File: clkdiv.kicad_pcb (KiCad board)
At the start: 2 copper layers, 11 parts, among them J1 Conn_02x05_Odd_Even

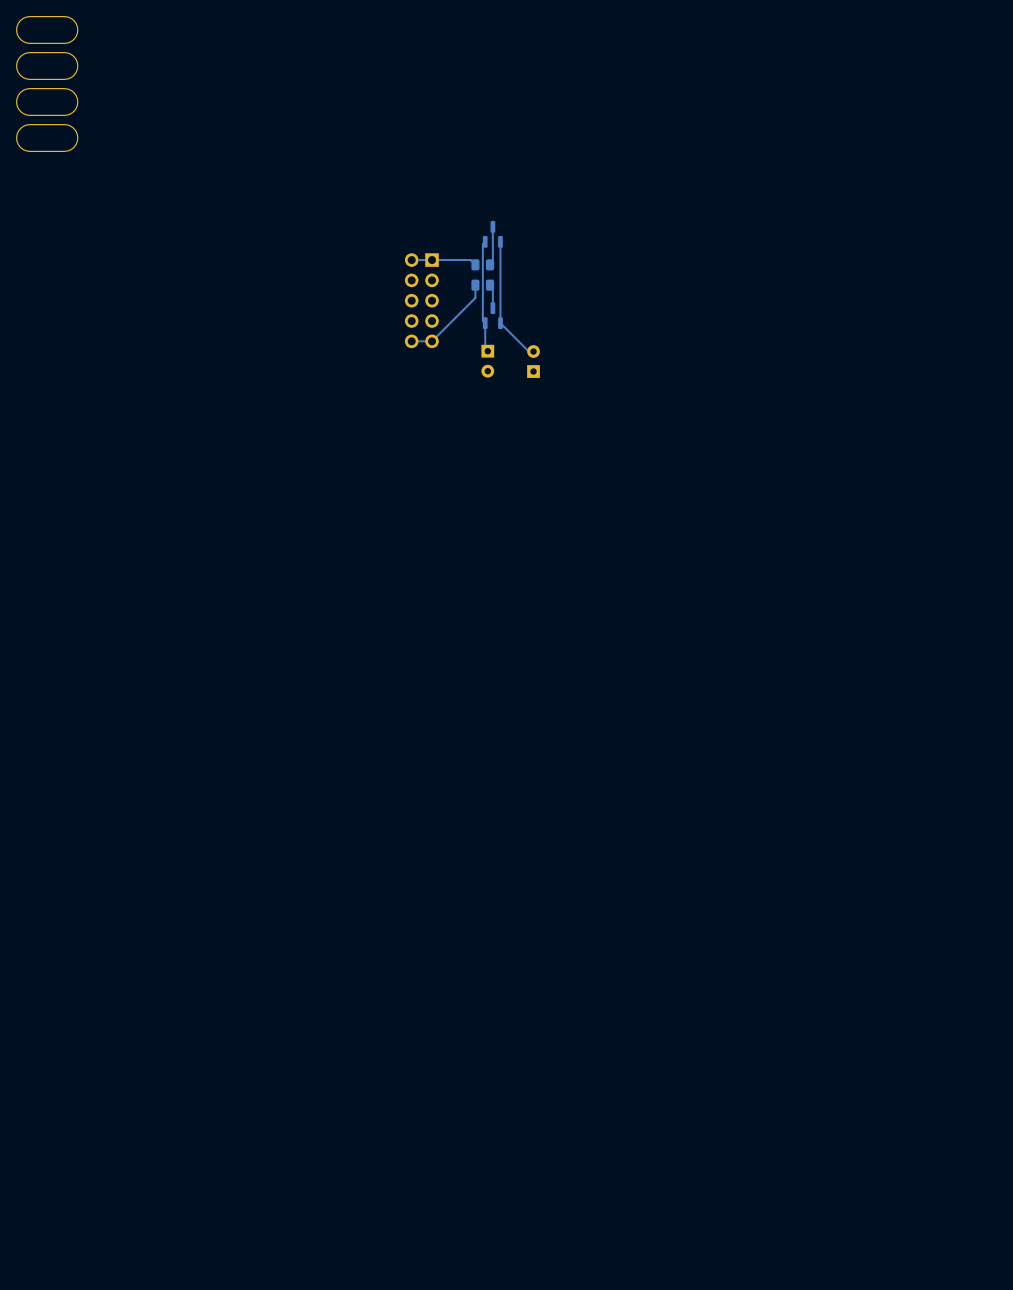
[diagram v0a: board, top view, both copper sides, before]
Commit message: pcb laid out, bom generated
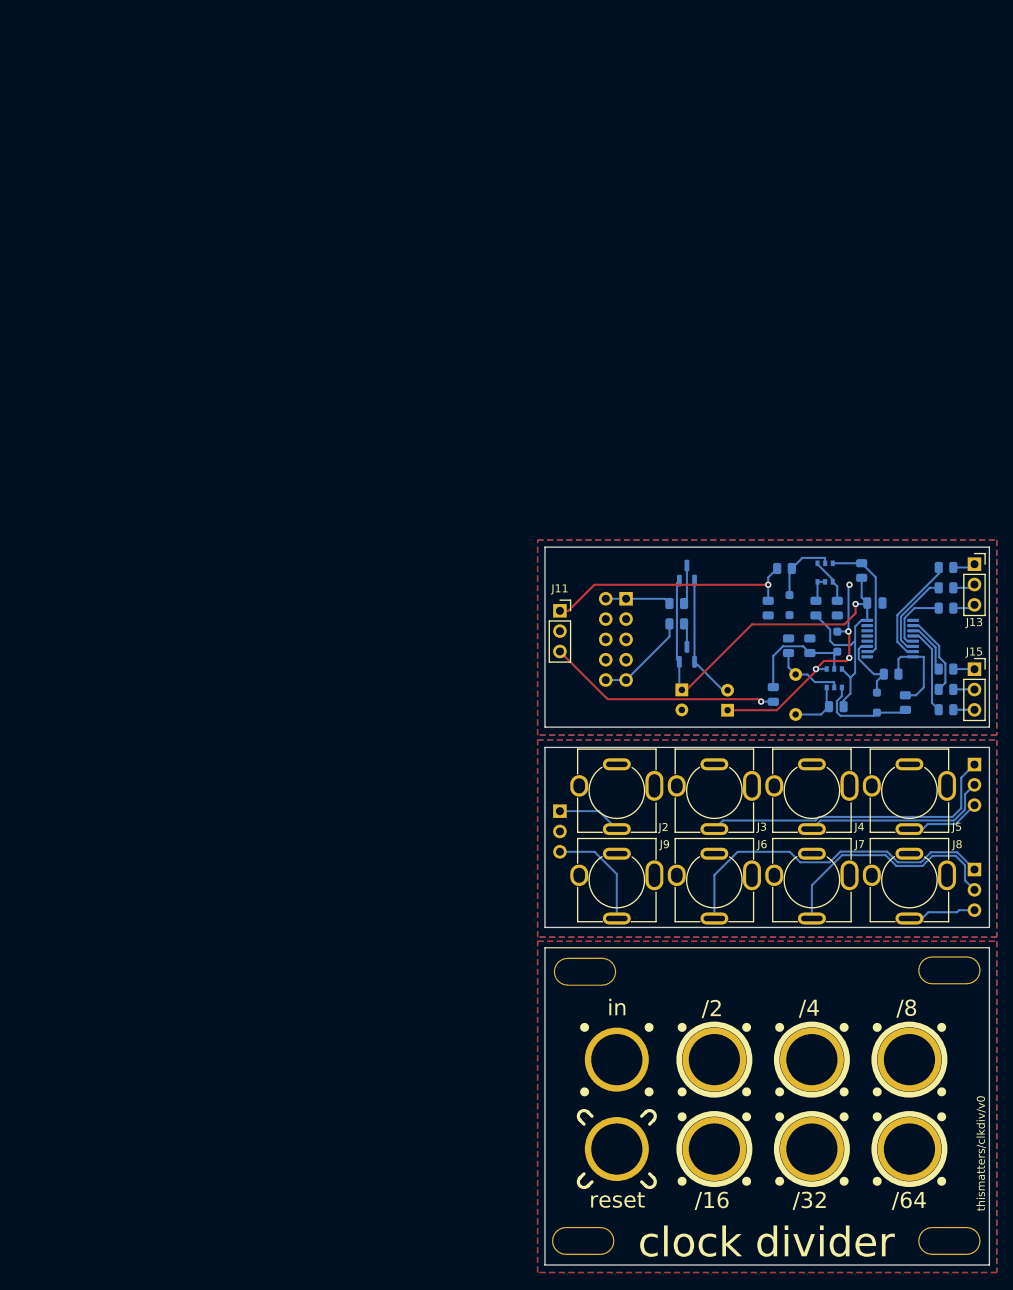
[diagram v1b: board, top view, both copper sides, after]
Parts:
- added C3: 100n, Capacitor_SMD:C_0805_2012Metric, B.Cu at (140.5, 88.6)
- added C4: 47n box, Capacitor_THT:C_Rect_L7.2mm_W2.5mm_P5.00mm_FKS2_FKP2_MKS2_MKP2, B.Cu at (130.6, 102.6)
- added D3: 1N4148, Diode_SMD:D_SOD-323_HandSoldering, B.Cu at (129.8, 88.9)
- added D4: 1N4148, Diode_SMD:D_SOD-323_HandSoldering, B.Cu at (135.8, 93.5)
- added D5: 1N4148, Diode_SMD:D_SOD-323_HandSoldering, B.Cu at (140.7, 101.1)
- added H10: 1/32, Eurorack:Mech-AudioJack-Hole-Output-Clock, F.Cu at (132.6, 156.9)
- added H11: 1/64, Eurorack:Mech-AudioJack-Hole-Output-Clock, F.Cu at (144.8, 156.9)
- added H12: reset, Eurorack:Mech-AudioJack-Hole-Input-Gate, F.Cu at (108.2, 156.9)
- added H5: in, Eurorack:Mech-AudioJack-Hole-Input-Clock, F.Cu at (108.2, 145.7)
- added H6: 1/2, Eurorack:Mech-AudioJack-Hole-Output-Clock, F.Cu at (120.4, 145.7)
- added H7: 1/4, Eurorack:Mech-AudioJack-Hole-Output-Clock, F.Cu at (132.6, 145.7)
- added H8: 1/8, Eurorack:Mech-AudioJack-Hole-Output-Clock, F.Cu at (144.8, 145.7)
- added H9: 1/16, Eurorack:Mech-AudioJack-Hole-Output-Clock, F.Cu at (120.4, 156.9)
- added J10: Conn_01x03_Pin, Connector_PinHeader_2.54mm:PinHeader_1x03_P2.54mm_Vertical, B.Cu at (101.1, 114.6)
- added J11: Conn_01x03_Socket, Connector_PinSocket_2.54mm:PinSocket_1x03_P2.54mm_Vertical, F.Cu at (101.1, 89.6)
- added J12: Conn_01x03_Pin, Connector_PinHeader_2.54mm:PinHeader_1x03_P2.54mm_Vertical, B.Cu at (152.9, 108.8)
- added J13: Conn_01x03_Socket, Connector_PinSocket_2.54mm:PinSocket_1x03_P2.54mm_Vertical, F.Cu at (152.9, 83.8)
- added J14: Conn_01x03_Pin, Connector_PinHeader_2.54mm:PinHeader_1x03_P2.54mm_Vertical, B.Cu at (152.9, 121.9)
- added J15: Conn_01x03_Socket, Connector_PinSocket_2.54mm:PinSocket_1x03_P2.54mm_Vertical, F.Cu at (152.9, 96.9)
- added J2: AudioJack2_SwitchT, Eurorack:AudioJack2_Tayda_A-2566, F.Cu at (108.2, 112.1)
- added J3: AudioJack2_SwitchT, Eurorack:AudioJack2_Tayda_A-2566, F.Cu at (120.4, 112.1)
- added J4: AudioJack2_SwitchT, Eurorack:AudioJack2_Tayda_A-2566, F.Cu at (132.6, 112.1)
- added J5: AudioJack2_SwitchT, Eurorack:AudioJack2_Tayda_A-2566, F.Cu at (144.8, 112.1)
- added J6: AudioJack2_SwitchT, Eurorack:AudioJack2_Tayda_A-2566, F.Cu at (120.4, 123.3)
- added J7: AudioJack2_SwitchT, Eurorack:AudioJack2_Tayda_A-2566, F.Cu at (132.6, 123.3)
- added J8: AudioJack2_SwitchT, Eurorack:AudioJack2_Tayda_A-2566, F.Cu at (144.8, 123.3)
- added J9: AudioJack2_SwitchT, Eurorack:AudioJack2_Tayda_A-2566, F.Cu at (108.2, 123.3)
- added Q3: BCM847, Package_SO:TSOP-6_1.65x3.05mm_P0.95mm, B.Cu at (134.2, 84.8)
- added Q4: BCM847, Package_SO:TSOP-6_1.65x3.05mm_P0.95mm, B.Cu at (135.4, 98.0)
- added R10: 10K, Resistor_SMD:R_0805_2012Metric, B.Cu at (135.6, 101.6)
- added R11: 220K, Resistor_SMD:R_0805_2012Metric, B.Cu at (129.7, 94.0)
- added R12: 22K, Resistor_SMD:R_0805_2012Metric, B.Cu at (144.3, 101.1)
- added R13: 1K, Resistor_SMD:R_0805_2012Metric, B.Cu at (149.4, 84.2)
- added R14: 1K, Resistor_SMD:R_0805_2012Metric, B.Cu at (149.4, 86.7)
- added R15: 1K, Resistor_SMD:R_0805_2012Metric, B.Cu at (149.4, 89.3)
- added R16: 1K, Resistor_SMD:R_0805_2012Metric, B.Cu at (149.4, 96.9)
- added R17: 1K, Resistor_SMD:R_0805_2012Metric, B.Cu at (149.4, 99.4)
- added R18: 1K, Resistor_SMD:R_0805_2012Metric, B.Cu at (149.4, 102.0)
- added R19: 1K, Resistor_SMD:R_0805_2012Metric, B.Cu at (142.5, 97.5)
- added R3: 1M, Resistor_SMD:R_0805_2012Metric, B.Cu at (127.1, 89.3)
- added R4: 1.2M, Resistor_SMD:R_0805_2012Metric, B.Cu at (129.2, 84.3)
- added R5: 22K, Resistor_SMD:R_0805_2012Metric, B.Cu at (133.1, 89.3)
- added R6: 22K, Resistor_SMD:R_0805_2012Metric, B.Cu at (138.8, 84.6)
- added R7: 220, Resistor_SMD:R_0805_2012Metric, B.Cu at (135.8, 89.3)
- added R8: 100K, Resistor_SMD:R_0805_2012Metric, B.Cu at (127.8, 100.1)
- added R9: 1M, Resistor_SMD:R_0805_2012Metric, B.Cu at (132.3, 94.0)
- added U1: 4040, Package_SO:TSSOP-16_4.4x5mm_P0.65mm, B.Cu at (142.4, 93.1)
- moved H3 181.6 mm to (149.8, 168.4)
- moved H2 159.7 mm to (149.8, 134.5)
- moved H4 153.3 mm to (104.0, 168.4)
- moved H1 135.6 mm to (104.2, 134.7)
- moved R1 48.8 mm to (115.7, 91.2)
- moved R2 48.8 mm to (115.7, 88.7)
- moved C1 48.8 mm to (116.3, 99.5)
- moved C2 48.8 mm to (122.0, 102.0)
- moved D1 48.8 mm to (117.0, 84.9)
- moved D2 48.8 mm to (117.0, 95.0)
- moved J1 48.8 mm to (109.4, 88.1)
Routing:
- net +12V: track 14.0 -> 68.3 mm, vias 0 -> 1
- net /BY16': track 0.00 -> 42.2 mm
- net GND: track 0.00 -> 41.7 mm, vias 0 -> 4
- net /BY2': track 0.00 -> 38.1 mm
- net /IN: track 0.00 -> 31.9 mm, vias 0 -> 1
- net /BY32': track 0.00 -> 30.0 mm
- net /RESET: track 0.00 -> 29.2 mm, vias 0 -> 1
- net /BY4': track 0.00 -> 23.7 mm
- net Net-(Q3B-C2): track 0.00 -> 16.2 mm
- net Net-(D4-K): track 0.00 -> 14.9 mm
- net Net-(U1-Q1): track 0.00 -> 13.9 mm
- net /RESET': track 0.00 -> 13.8 mm
- net Net-(D5-A): track 0.00 -> 11.9 mm
- net Net-(U1-Q2): track 0.00 -> 11.0 mm
- net Net-(U1-Q6): track 0.00 -> 11.0 mm
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- added copper zone on B.Cu, net /FACE
- added copper zone on F.Cu, net /FACE
- added copper zone on B.Cu, net /GND'
- added copper zone on F.Cu, net /GND'
- added copper zone on B.Cu, net GND
- added copper zone on F.Cu, net GND
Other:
- board outline added: 55.6 x 89.7 mm
- board text added: "/16"
- board text added: "/2"
- board text added: "/32"
- board text added: "/4"
- board text added: "/64"
- board text added: "/8"
- board text added: "clock divider"
- board text added: "in"
- board text added: "reset"
- board text added: "thismatters/clkdiv/v0"
